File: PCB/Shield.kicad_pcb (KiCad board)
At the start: 2 copper layers, 80 x 69.2 mm, 84 parts, among them J1 Screw_Terminal_01x04, J10 PWR SW, J14 SERVO1, J15 SERVO2, J16 SERVO3, J17 ENC1, J18 ENC2, J2 BATT, J20 SERVO4, J3 ADC, J4 ULTRA, J5 I2C, Q1 2N7002DWK, Q2 DualPMOS, Q4 Q_PMOS_GDS, Q5 Q_PMOS_GDS, SW1 PWR SW, SW2 SW_DIP_x01, U1 LMV331, U2 4077, U3 NCP1117-5.0_SOT223, U6 L298P, U7 LMV358

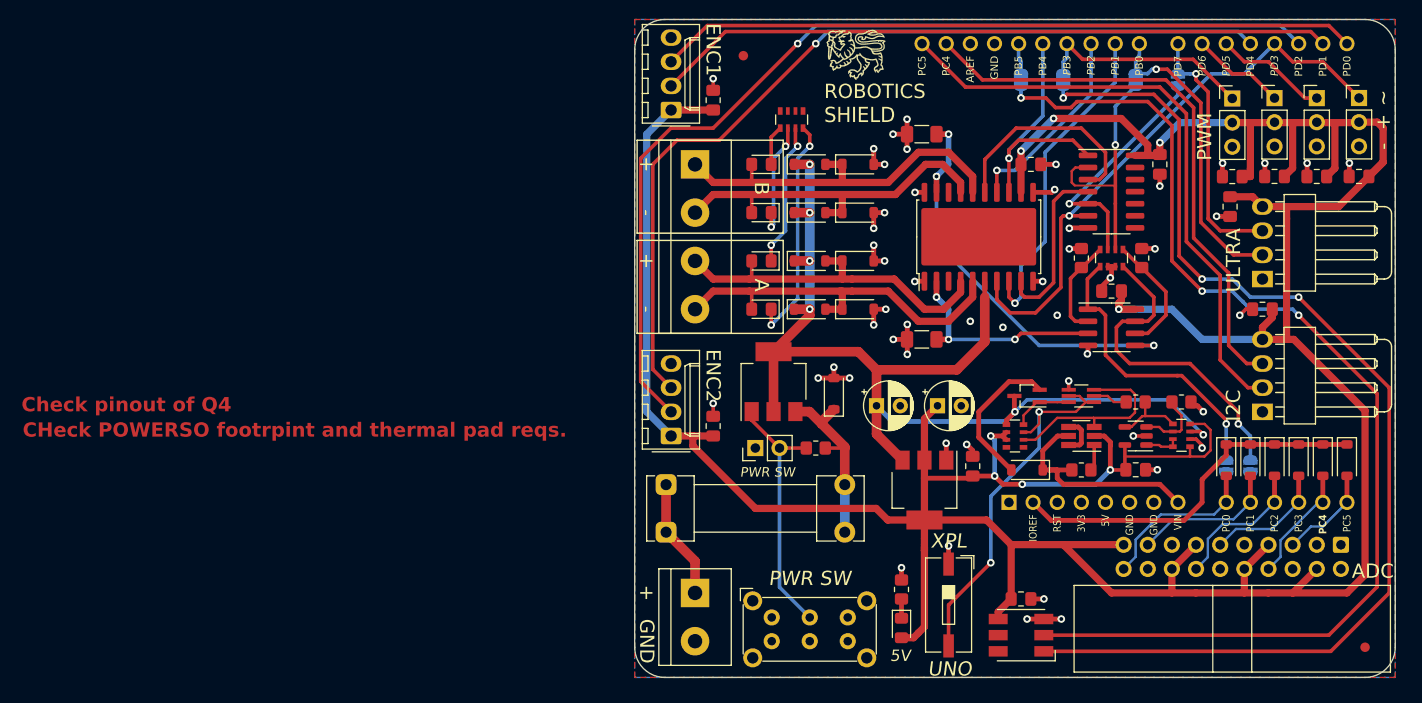
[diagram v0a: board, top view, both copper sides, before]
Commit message: Tidied schematic and layout, added indicators and silkscreen notes
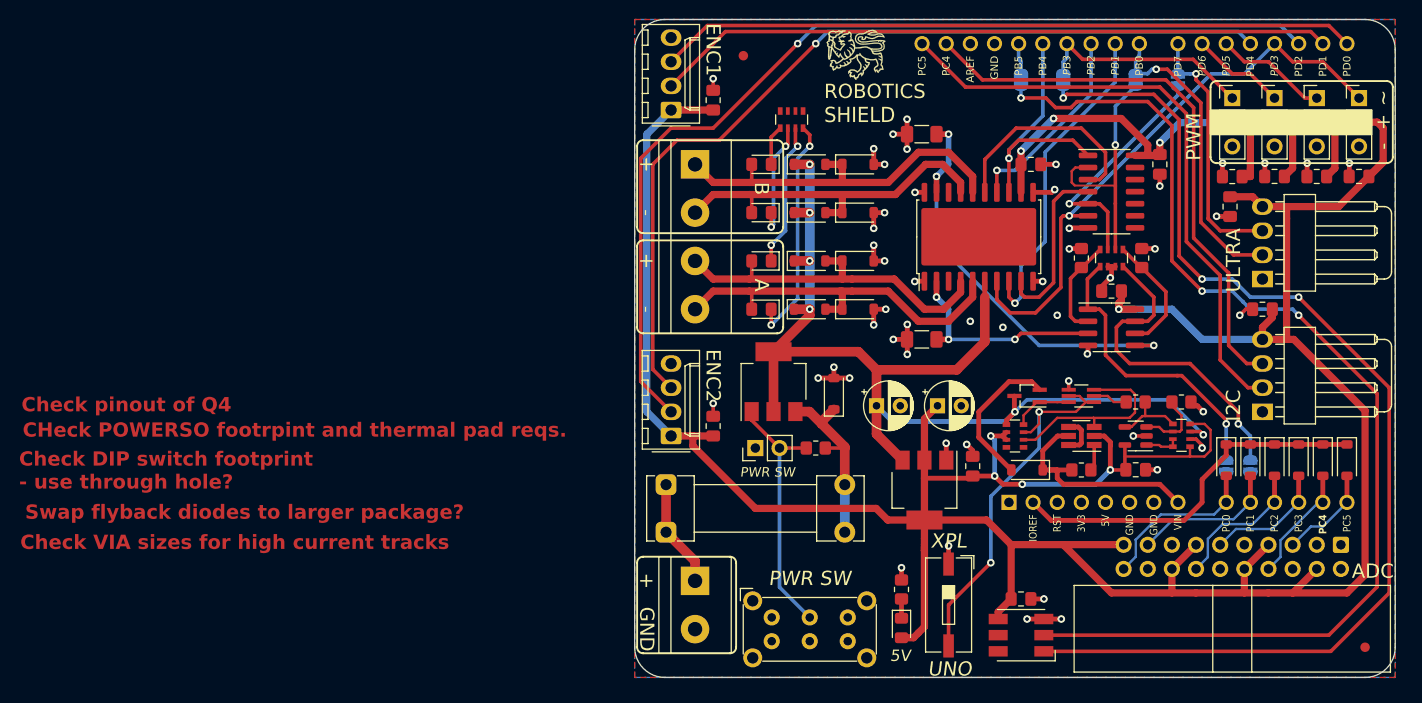
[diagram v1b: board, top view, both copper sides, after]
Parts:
- moved J2 1.27 mm to (102.2, 90.2)
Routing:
- net Net-(J2-Pin_1): track 12.7 -> 11.4 mm
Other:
- board text added: "Check DIP switch footprint - use through hole?"
- board text added: "Check VIA sizes for high current tracks"
- board text added: "Swap flyback diodes to larger package?"

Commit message: Fixed links between schem and pcb, re-added annotation, updated L298 footprint and updated layout
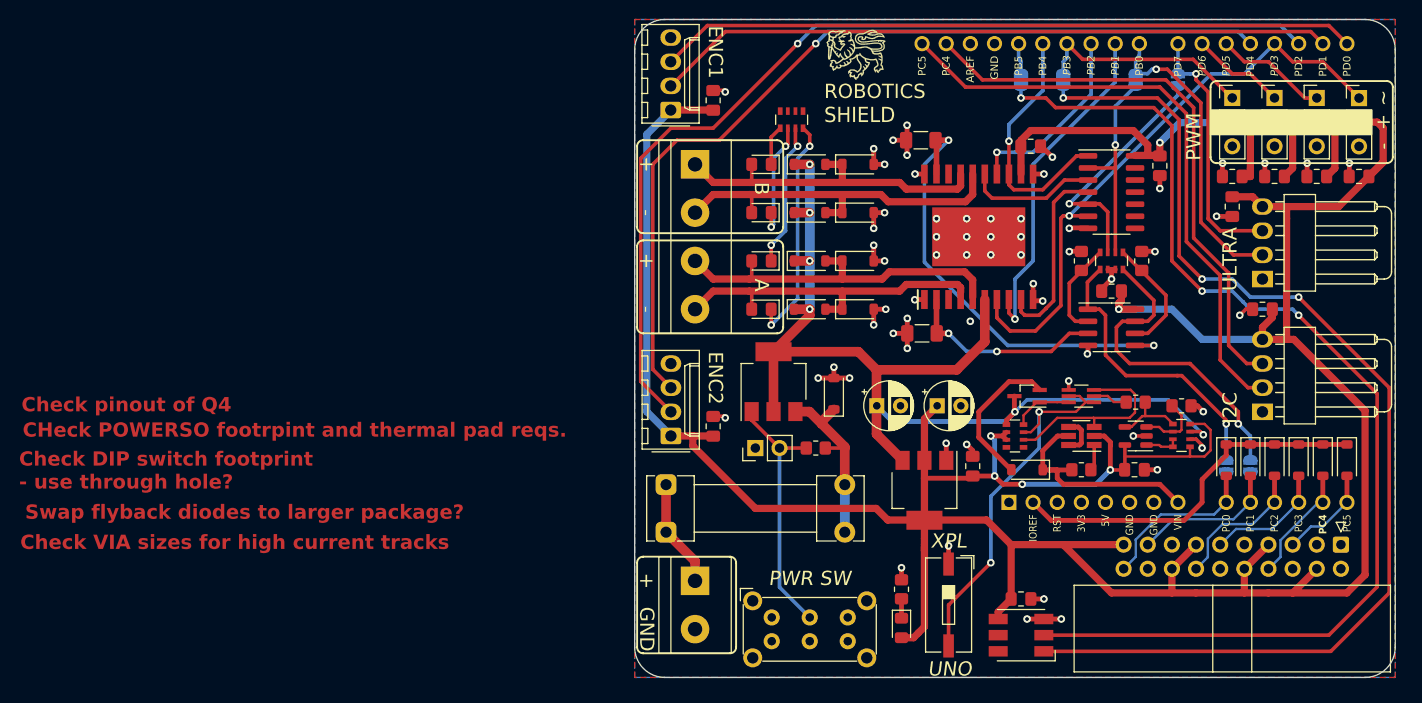
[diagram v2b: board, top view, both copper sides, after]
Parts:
- removed C17, C19: 100n, Capacitor_SMD:C_0805_2012Metric_Pad1.18x1.45mm_HandSolder
- removed C18: 10u, Capacitor_THT:CP_Radial_D5.0mm_P2.50mm
- removed D23: D, Diode_SMD:D_SOD-123
- removed J14: SERVO1, Connector_PinHeader_2.54mm:PinHeader_1x03_P2.54mm_Vertical
- removed J15: SERVO2, Connector_PinHeader_2.54mm:PinHeader_1x03_P2.54mm_Vertical
- removed J16: SERVO3, Connector_PinHeader_2.54mm:PinHeader_1x03_P2.54mm_Vertical
- removed J17: ENC1, Connector_Molex:Molex_KK-254_AE-6410-04A_1x04_P2.54mm_Vertical
- removed J18: ENC2, Connector_Molex:Molex_KK-254_AE-6410-04A_1x04_P2.54mm_Vertical
- removed J20: SERVO4, Connector_PinHeader_2.54mm:PinHeader_1x03_P2.54mm_Vertical
- removed JP7, JP8: SolderJumper_2_Open, Jumper:SolderJumper-2_P1.3mm_Open_RoundedPad1.0x1.5mm
- removed Q5: Q_PMOS_GDS, Package_TO_SOT_SMD:SOT-323_SC-70_Handsoldering
- removed R14: 150R, Resistor_SMD:R_0805_2012Metric_Pad1.20x1.40mm_HandSolder
- removed R15: 10k, Resistor_SMD:R_0805_2012Metric_Pad1.20x1.40mm_HandSolder
- removed R16, R17: 0R15, Resistor_SMD:R_1206_3216Metric_Pad1.30x1.75mm_HandSolder
- removed R18, R20: 1K, Resistor_SMD:R_0805_2012Metric_Pad1.20x1.40mm_HandSolder
- removed R29, R35: 100R, Resistor_SMD:R_0805_2012Metric_Pad1.20x1.40mm_HandSolder
- removed R32: 2K5, Resistor_SMD:R_0805_2012Metric_Pad1.20x1.40mm_HandSolder
- removed REF** (x2): Fiducial_1mm_Mask2mm, Fiducial:Fiducial_1mm_Mask2mm
- removed U6: L298P, Package_SO:SO-20-1EP_7.52x12.825mm_P1.27mm_EP6.045x12.09mm_Mask3.56x4.47mm
- removed U7: LMV358, Package_SO:SOIC-8_3.9x4.9mm_P1.27mm
- added C2: 100u, Capacitor_THT:CP_Radial_D5.0mm_P2.50mm, F.Cu at (121.3, 71.8)
- added C3: 100n, Capacitor_SMD:C_0805_2012Metric_Pad1.18x1.45mm_HandSolder, F.Cu at (137.5, 44.5)
- added C4: C, Capacitor_SMD:C_0805_2012Metric_Pad1.18x1.45mm_HandSolder, F.Cu at (131.4, 78.1)
- added D1: D, Diode_SMD:D_SOD-123, F.Cu at (158.1, 77.5)
- added J11: SERVO3, Connector_PinHeader_2.54mm:PinHeader_1x03_P2.54mm_Vertical, F.Cu at (158.8, 39.4)
- added J12: SERVO4, Connector_PinHeader_2.54mm:PinHeader_1x03_P2.54mm_Vertical, F.Cu at (172.1, 39.4)
- added J6: ULTRA, footprints:Molex_KK-254_1x04_P2.54mm_Horizontal, F.Cu at (161.9, 58.4)
- added J7: ENC1, Connector_Molex:Molex_KK-254_AE-6410-04A_1x04_P2.54mm_Vertical, F.Cu at (99.7, 40.6)
- added J8: SERVO2, Connector_PinHeader_2.54mm:PinHeader_1x03_P2.54mm_Vertical, F.Cu at (163.2, 39.4)
- added J9: ENC2, Connector_Molex:Molex_KK-254_AE-6410-04A_1x04_P2.54mm_Vertical, F.Cu at (99.7, 74.9)
- added JP1: SolderJumper_2_Open, Jumper:SolderJumper-2_P1.3mm_Open_RoundedPad1.0x1.5mm, B.Cu at (153.0, 37.5)
- added JP2: SolderJumper_2_Open, Jumper:SolderJumper-2_P1.3mm_Open_RoundedPad1.0x1.5mm, B.Cu at (148.6, 37.5)
- added Q3: Q_PMOS_GDS, Package_TO_SOT_SMD:SOT-323_SC-70_Handsoldering, F.Cu at (137.2, 70.7)
- added R1: 10k, Resistor_SMD:R_0805_2012Metric_Pad1.20x1.40mm_HandSolder, F.Cu at (114.9, 76.2)
- added R2: 0R15, Resistor_SMD:R_1206_3216Metric_Pad1.30x1.75mm_HandSolder, F.Cu at (126.1, 64.1)
- added R3: 0R15, Resistor_SMD:R_1206_3216Metric_Pad1.30x1.75mm_HandSolder, F.Cu at (126.0, 43.8)
- added R4: 150R, Resistor_SMD:R_0805_2012Metric_Pad1.20x1.40mm_HandSolder, F.Cu at (124.0, 91.1)
- added R5: 2K5, Resistor_SMD:R_0805_2012Metric_Pad1.20x1.40mm_HandSolder, F.Cu at (153.4, 71.8)
- added R6: 100R, Resistor_SMD:R_0805_2012Metric_Pad1.20x1.40mm_HandSolder, F.Cu at (148.6, 71.4)
- added R7: 100R, Resistor_SMD:R_0805_2012Metric_Pad1.20x1.40mm_HandSolder, F.Cu at (142.9, 78.5)
- added R8: 1K, Resistor_SMD:R_0805_2012Metric_Pad1.20x1.40mm_HandSolder, F.Cu at (142.9, 56.5)
- added R9: 1K, Resistor_SMD:R_0805_2012Metric_Pad1.20x1.40mm_HandSolder, F.Cu at (149.2, 56.5)
- added U4: LMV331, Package_TO_SOT_SMD:SOT-23-5, F.Cu at (148.6, 74.9)
- added U5: LMV358, Package_SO:SOIC-8_3.9x4.9mm_P1.27mm, F.Cu at (146.1, 63.5)
- C5: value 100u -> 10u
- C6: value C -> 100n
- D10: value D -> 5V; footprint Diode_SMD:D_SOD-123 -> LED_SMD:LED_0805_2012Metric_Pad1.15x1.40mm_HandSolder
- D12, D13, D14, D15: value LED -> D; footprint LED_SMD:LED_0805_2012Metric_Pad1.15x1.40mm_HandSolder -> Diode_SMD:D_SOD-123
- D17, D18, D19, D20: value D -> LED; footprint Diode_SMD:D_SOD-123 -> LED_SMD:LED_0805_2012Metric_Pad1.15x1.40mm_HandSolder
- D3: value 5V -> D; footprint LED_SMD:LED_0805_2012Metric_Pad1.15x1.40mm_HandSolder -> Diode_SMD:D_SOD-123
- J1: value Screw_Terminal_01x04 -> ADC; footprint TerminalBlock:TerminalBlock_bornier-4_P5.08mm -> Connector_IDC:IDC-Header_2x10_P2.54mm_Horizontal
- J10: value PWR SW -> I2C; footprint Connector_PinHeader_2.54mm:PinHeader_1x02_P2.54mm_Vertical -> footprints:Molex_KK-254_1x04_P2.54mm_Horizontal
- J3: value ADC -> PWR SW; footprint Connector_IDC:IDC-Header_2x10_P2.54mm_Horizontal -> Connector_PinHeader_2.54mm:PinHeader_1x02_P2.54mm_Vertical
- J4: value ULTRA -> Screw_Terminal_01x04; footprint footprints:Molex_KK-254_1x04_P2.54mm_Horizontal -> TerminalBlock:TerminalBlock_bornier-4_P5.08mm
- J5: value I2C -> SERVO1; footprint footprints:Molex_KK-254_1x04_P2.54mm_Horizontal -> Connector_PinHeader_2.54mm:PinHeader_1x03_P2.54mm_Vertical
- Q1: value 2N7002DWK -> Q_PMOS_GDS; footprint Package_TO_SOT_SMD:SOT-363_SC-70-6_Handsoldering -> Package_TO_SOT_SMD:SOT-223-3_TabPin2
- Q2: value DualPMOS -> 2N7002DWK; footprint Package_TO_SOT_SMD:SOT-23-6_Handsoldering -> Package_TO_SOT_SMD:SOT-363_SC-70-6_Handsoldering
- Q4: value Q_PMOS_GDS -> DualPMOS; footprint Package_TO_SOT_SMD:SOT-223-3_TabPin2 -> Package_TO_SOT_SMD:SOT-23-6_Handsoldering
- RN2: value 10K -> 10k
- RN3: value 10k -> 10K
- U1: value LMV331 -> 4077; footprint Package_TO_SOT_SMD:SOT-23-5 -> Package_SO:SOIC-14_3.9x8.7mm_P1.27mm
- U2: value 4077 -> NCP1117-5.0_SOT223; footprint Package_SO:SOIC-14_3.9x8.7mm_P1.27mm -> Package_TO_SOT_SMD:SOT-223-3_TabPin2
- U3: value NCP1117-5.0_SOT223 -> L298P; footprint Package_TO_SOT_SMD:SOT-223-3_TabPin2 -> footprints:SOIC127P1420X360-21N
- moved J1 78.8 mm to (170.2, 86.4)
- moved C14 72.8 mm to (172.1, 47.6), turned to 180 degrees
- moved C10 68.7 mm to (104.1, 73.9), turned to 90 degrees
- moved D20 66.8 mm to (109.2, 46.4), turned to 180 degrees
- moved J3 62.4 mm to (108.6, 76.2), turned to 90 degrees
- moved D19 62.2 mm to (109.2, 51.4), turned to 180 degrees
- moved C8 61.8 mm to (104.1, 39.6), turned to 90 degrees
- moved J4 60.9 mm to (102.2, 46.4), turned to -90 degrees
- moved D6 58.0 mm to (168.3, 77.5), turned to -90 degrees
- moved D18 57.9 mm to (109.2, 56.5), turned to 180 degrees
- moved D7 57.6 mm to (170.8, 77.5), turned to -90 degrees
- moved C15 56.9 mm to (136.5, 92.1)
- moved C13 55.2 mm to (158.8, 47.6), turned to 180 degrees
- moved D17 53.8 mm to (109.2, 61.6), turned to 180 degrees
- moved J10 53.5 mm to (161.9, 72.4)
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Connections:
- net /uC/uC_3V3 renamed /uC_3V3
- net /uC/uC_5V renamed /uC_5V
- A1 pad 10: /uC/AIN1 -> /AIN1
- A1 pad 11: /uC/AIN2 -> /AIN2
- A1 pad 12: /uC/AIN3 -> /AIN3
- A1 pad 13: /uC/AIN4 -> /AIN4
- A1 pad 14: /uC/AIN5 -> /AIN5
- A1 pad 15: /uC/ENC1B -> /ENC1B
- A1 pad 16: /uC/ENC1A -> /ENC1A
- A1 pad 17: /uC/ENC2A -> /ENC2A
- A1 pad 18: /uC/DIRA -> /DIRA
- A1 pad 19: /uC/ENC2B -> /ENC2B
- A1 pad 2: /uC/IOREF -> /IOREF
- A1 pad 20: /uC/SERVO1 -> /SERVO1
- A1 pad 21: /uC/SERVO2 -> /SERVO2
- A1 pad 22: /uC/BRKA -> /BRKA
- A1 pad 23: /uC/BRKB -> /BRKB
- A1 pad 24: /uC/MTRA -> /MTRA
- A1 pad 25: /uC/MTRB -> /MTRB
- A1 pad 26: /uC/MOSI -> /MOSI
- A1 pad 27: /uC/DIRB -> /DIRB
- A1 pad 28: /uC/SCK -> /SCK
- A1 pad 31: /uC/SCL -> /SCL
- A1 pad 32: /uC/SDA -> /SDA
- A1 pad 8: /uC/Vin -> /Vin
- A1 pad 9: /uC/AIN0 -> /AIN0
- C15 pad 1: +5V -> GND
- C15 pad 2: GND -> +5V
- C5 pad 1: +BATT -> +5V
- C7 pad 1: GND -> +5V
- C7 pad 2: +5V -> GND
- D10 pad 1: +BATT -> Net-(D10-K)
- D10 pad 2: Net-(D10-A) -> +5V
- D12 pad 1: Net-(D12-K) -> Net-(D11-A)
- D12 pad 2: Net-(D12-A) -> GND
- D13 pad 1: Net-(D13-K) -> +BATT
- D14 pad 1: Net-(D14-K) -> Net-(D13-A)
- D14 pad 2: Net-(D10-A) -> GND
- D15 pad 1: Net-(D15-K) -> +BATT
- D15 pad 2: Net-(D11-A) -> Net-(D15-A)
- D16 pad 1: /uC/IOREF -> Net-(D15-A)
- D16 pad 2: /uC/AIN0 -> GND
- D17 pad 1: /uC/IOREF -> Net-(D17-K)
- D17 pad 2: /uC/AIN1 -> Net-(D17-A)
- D18 pad 1: /uC/IOREF -> Net-(D18-K)
- D18 pad 2: /uC/AIN2 -> Net-(D11-A)
- D19 pad 1: /uC/IOREF -> Net-(D19-K)
- D19 pad 2: /uC/AIN3 -> Net-(D13-A)
- D2 pad 1: Net-(D2-K) -> /IOREF
- D2 pad 2: GND -> /AIN1
- D20 pad 1: /uC/IOREF -> Net-(D20-K)
- D20 pad 2: /uC/AIN4 -> Net-(D15-A)
- D21 pad 1: /uC/IOREF -> /Vin
- D21 pad 2: /uC/AIN5 -> Net-(D21-A)
- D3 pad 1: Net-(D3-K) -> /IOREF
- D3 pad 2: +5V -> /AIN2
- D4 pad 1: Net-(D12-A) -> Net-(D4-K)
- D5 pad 1: Net-(D13-A) -> /IOREF
- D5 pad 2: GND -> /AIN3
- D6 pad 1: Net-(D10-A) -> /IOREF
- D6 pad 2: GND -> /AIN4
- D7 pad 1: Net-(D11-A) -> /IOREF
- D7 pad 2: GND -> /AIN5
- D8 pad 2: Net-(D12-A) -> Net-(D17-A)
- D9 pad 1: +BATT -> Net-(D17-A)
- D9 pad 2: Net-(D13-A) -> GND
- F1 pad 2: Net-(D2-K) -> Net-(D4-K)
- J1 pad 1: Net-(D10-A) -> GND
- J1 pad 2: Net-(D11-A) -> GND
- J1 pad 3: Net-(D12-A) -> GND
- J1 pad 4: Net-(D13-A) -> +5V
- J10 pad 2: Net-(J10-Pin_2) -> /SDA
- J3 pad 2: GND -> Net-(J3-Pin_2)
- J4 pad 1: GND -> Net-(D15-A)
- J4 pad 2: /uC/BRKB -> Net-(D13-A)
- J4 pad 3: /uC/BRKA -> Net-(D11-A)
- J4 pad 4: +5V -> Net-(D17-A)
- J5 pad 1: GND -> /SERVO1
- J5 pad 2: /uC/SDA -> +5V
- J5 pad 3: /uC/SCL -> GND
- JP3 pad 1: /uC/MTR_A_SNS -> /MOSI
- JP3 pad 2: /uC/AIN0 -> Net-(D22-DI)
- JP4 pad 1: /uC/MTR_B_SNS -> /SCK
- JP4 pad 2: /uC/AIN1 -> Net-(D22-CI)
- JP5 pad 1: /uC/BRKB -> Net-(JP5-A)
- JP5 pad 2: Net-(JP5-B) -> /AIN0
- JP6 pad 1: /uC/BRKA -> Net-(JP6-A)
- JP6 pad 2: Net-(JP6-B) -> /AIN1
- Q1 pad 1: Net-(Q1A-S) -> Net-(J3-Pin_2)
- Q1 pad 2: Net-(Q1A-G) -> +BATT
- Q1 pad 3: Net-(Q1B-D) -> Net-(D4-K)
- Q2 pad 1: Net-(Q2A-G) -> Net-(Q2A-S)
- Q2 pad 2: +5V -> Net-(Q2A-G)
- Q2 pad 3: Net-(Q1B-D) -> Net-(Q2B-D)
- Q2 pad 4: Net-(Q2A-D) -> GND
- Q2 pad 5: /uC/Vin -> Net-(Q2A-S)
- Q4 pad 1: Net-(J10-Pin_2) -> Net-(Q4A-G)
- Q4 pad 2: +BATT -> +5V
- Q4 pad 3: Net-(D2-K) -> Net-(Q2B-D)
- RN1 pad 1: GND -> Net-(RN1A-R1.1)
- RN1 pad 2: GND -> Net-(JP2-B)
- RN1 pad 3: GND -> Net-(JP1-B)
- RN1 pad 4: GND -> Net-(RN1D-R4.1)
- RN1 pad 5: Net-(D14-K) -> Net-(JP5-A)
- RN1 pad 6: Net-(D15-K) -> GND
- RN1 pad 7: Net-(D12-K) -> GND
- RN1 pad 8: Net-(D13-K) -> Net-(JP6-A)
- RN2 pad 1: Net-(RN2A-R1.1) -> +5V
- RN2 pad 2: Net-(JP5-B) -> GND
- RN2 pad 3: Net-(JP6-B) -> +BATT
- RN2 pad 4: Net-(RN2D-R4.1) -> +5V
- RN2 pad 5: /uC/MTR_A_SNS -> Net-(RN2D-R4.2)
- RN2 pad 6: GND -> Net-(RN2C-R3.2)
- RN2 pad 7: GND -> Net-(RN2A-R1.2)
- RN2 pad 8: /uC/MTR_B_SNS -> Net-(RN2A-R1.2)
- RN3 pad 1: +5V -> GND
- RN3 pad 3: +BATT -> GND
- RN3 pad 4: +5V -> GND
- RN3 pad 5: Net-(RN3D-R4.2) -> Net-(D20-K)
- RN3 pad 6: Net-(RN3C-R3.2) -> Net-(D19-K)
- RN3 pad 7: Net-(RN3A-R1.2) -> Net-(D18-K)
- RN3 pad 8: Net-(RN3A-R1.2) -> Net-(D17-K)
- RN4 pad 2: Net-(Q1B-D) -> Net-(Q2B-D)
- RN4 pad 3: Net-(Q1A-S) -> Net-(Q2A-S)
- RN4 pad 4: Net-(Q1A-D) -> Net-(Q2A-D)
- SW1 pad 2: Net-(J10-Pin_2) -> Net-(J3-Pin_2)
- SW2 pad 2: Net-(Q1A-S) -> Net-(Q2A-S)
- U1 pad 1: Net-(RN3A-R1.2) -> /DIRB
- U1 pad 2: GND -> Net-(JP2-B)
- U1 pad 3: Net-(RN3C-R3.2) -> Net-(U3-IN4)
- U1 pad 4: Net-(RN3D-R4.2) -> Net-(U3-IN2)
- U1 pad 5: +5V -> Net-(JP1-B)
- U2 pad 1: /uC/DIRB -> GND
- U2 pad 2: Net-(JP5-B) -> +5V
- U2 pad 3: Net-(U6-IN4) -> +BATT
- U3 pad 2: +5V -> /SENA
- U3 pad 3: +BATT -> unconnected-(U3-NC-Pad3)
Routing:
- net /uC/ENC2A: track 103.8 -> 0.00 mm, vias 1 -> 0
- net /ENC2A: track 0.00 -> 103.8 mm, vias 0 -> 1
- net /uC/ENC2B: track 93.5 -> 0.00 mm, vias 1 -> 0
- net /ENC2B: track 0.00 -> 93.5 mm, vias 0 -> 1
- net /uC/ENC1B: track 73.5 -> 0.00 mm
- net /ENC1B: track 0.00 -> 73.5 mm
- net /uC/ENC1A: track 71.5 -> 0.00 mm
- net /ENC1A: track 0.00 -> 71.5 mm
- net /uC/SDA: track 63.9 -> 0.00 mm
- net /SDA: track 0.00 -> 63.9 mm
- net /DIRA: track 0.00 -> 62.8 mm, vias 0 -> 1
- net /uC/DIRA: track 60.9 -> 0.00 mm, vias 1 -> 0
- net /uC/SCL: track 59.7 -> 0.00 mm
- net /SCL: track 0.00 -> 59.7 mm
- net /SENB: track 0.00 -> 48.5 mm, vias 0 -> 2
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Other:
- board text added: "ENC1"
- board text added: "ENC2"
- board text added: "I2C"
- board text added: "ULTRA"
